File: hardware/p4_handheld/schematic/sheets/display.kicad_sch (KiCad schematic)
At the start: 0 parts

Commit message: hw(p4_handheld): display sheet wired to Waveshare 2.8in DSI panel
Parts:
- added C3: 10u, C0603, symbol Device:C
- added J3: FFC-15-1.0-FH12-class, FPC-SMD_FH12-15S-0.5SH-55, symbol PSP4H:Block2
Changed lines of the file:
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@@
     (comment 2 "Same-net labels connect; globals cross sheets")
   )
+  (symbol (lib_id "PSP4H:Block2") (at 35 35 0) (unit 1)
+    (exclude_from_sim no) (in_bom yes) (on_board yes) (dnp no) (fields_autoplaced)
+    (property "Reference" "J3" (at 35 29 0)
+      (effects (font (size 1.27 1.27))))
+    (property "Value" "FFC-15-1.0-FH12-class" (at 35 41 0)
+      (effects (font (size 1.27 1.27))))
+    (property "Footprint" "FPC-SMD_FH12-15S-0.5SH-55" (at 35 35 0)
+      (effects (font (size 1.27 1.27)) hide))
+    (property "Datasheet" "~" (at 35 35 0)
+      (effects (font (size 1.27 1.27)) hide))
+    (property "Gate" "GATE-PANEL-FFC-CONTACT" (at 35 35 0)
+      (effects (font (size 1.27 1.27)) hide))
+    (property "LCSC" "C2832207" (at 35 35 0)
+      (effects (font (size 1.27 1.27)) hide))
+    (property "MPN" "FH12-15S-0.5SH(55)" (at 35 35 0)
+      (effects (font (size 1.27 1.27)) hide))
+    (instances (project "card" (path "/p4_handheld/sheets/display" (reference "J3") (unit 1))))
+  )
+  (label "+3V3_PANEL" (at 53 32.5 0) (fields_autoplaced)
+    (effects (font (size 1.27 1.27)) (justify left)))
+  (label "+3V3_PANEL" (at 53 32.5 0) (fields_autoplaced)
+    (effects (font (size 1.27 1.27)) (justify left)))
+  (label "GND" (at 53 30 0) (fields_autoplaced)
+    (effects (font (size 1.27 1.27)) (justify left)))
+  (label "GND" (at 53 37.5 0) (fields_autoplaced)
+    (effects (font (size 1.27 1.27)) (justify left)))
+  (label "GND" (at 53 32.5 0) (fields_autoplaced)
+    (effects (font (size 1.27 1.27)) (justify left)))
+  (label "GND" (at 53 32.5 0) (fields_autoplaced)
+    (effects (font (size 1.27 1.27)) (justify left)))
+  (label "GND" (at 53 32.5 0) (fields_autoplaced)
+    (effects (font (size 1.27 1.27)) (justify left)))
+  (label "I2C_SDA" (at 53 32.5 0) (fields_autoplaced)
+    (effects (font (size 1.27 1.27)) (justify left)))
+  (label "I2C_SCL" (at 53 32.5 0) (fields_autoplaced)
+    (effects (font (size 1.27 1.27)) (justify left)))
+  (label "DSI_D1_N" (at 53 32.5 0) (fields_autoplaced)
+    (effects (font (size 1.27 1.27)) (justify left)))
+  (label "DSI_D1_P" (at 53 35 0) (fields_autoplaced)
+    (effects (font (size 1.27 1.27)) (justify left)))
+  (label "DSI_CLK_N" (at 53 40 0) (fields_autoplaced)
+    (effects (font (size 1.27 1.27)) (justify left)))
+  (label "DSI_CLK_P" (at 53 30 0) (fields_autoplaced)
+    (effects (font (size 1.27 1.27)) (justify left)))
+  (label "DSI_D0_N" (at 53 35 0) (fields_autoplaced)
+    (effects (font (size 1.27 1.27)) (justify left)))
+  (label "DSI_D0_P" (at 53 37.5 0) (fields_autoplaced)
+    (effects (font (size 1.27 1.27)) (justify left)))
+  (symbol (lib_id "Device:C") (at 80 35 0) (unit 1)
+    (exclude_from_sim no) (in_bom yes) (on_board yes) (dnp no) (fields_autoplaced)
+    (property "Reference" "C3" (at 80 29 0)
+      (effects (font (size 1.27 1.27))))
+    (property "Value" "10u" (at 80 41 0)
+      (effects (font (size 1.27 1.27))))
+    (property "Footprint" "C0603" (at 80 35 0)
+      (effects (font (size 1.27 1.27)) hide))
+    (property "Datasheet" "~" (at 80 35 0)
+      (effects (font (size 1.27 1.27)) hide))
+    (property "LCSC" "C19702" (at 80 35 0)
+      (effects (font (size 1.27 1.27)) hide))
+    (property "MPN" "CL10A106KP8NNNC" (at 80 35 0)
+      (effects (font (size 1.27 1.27)) hide))
+    (instances (project "card" (path "/p4_handheld/sheets/display" (reference "C3") (unit 1))))
+  )
+  (label "+3V3_PANEL" (at 98 30 0) (fields_autoplaced)
+    (effects (font (size 1.27 1.27)) (justify left)))
+  (label "GND" (at 98 32.5 0) (fields_autoplaced)
+    (effects (font (size 1.27 1.27)) (justify left)))
+  (global_label "+3V3_PANEL" (shape input) (at 280 20 0) (fields_autoplaced)
+    (effects (font (size 1.27 1.27)) (justify left))
+    (property "Intersheetrefs" "${INTERSHEET_REFS}" (at 280 20 0)
+      (effects (font (size 1.27 1.27)) hide))
+  )
+  (global_label "GND" (shape input) (at 280 26 0) (fields_autoplaced)
+    (effects (font (size 1.27 1.27)) (justify left))
+    (property "Intersheetrefs" "${INTERSHEET_REFS}" (at 280 26 0)
+      (effects (font (size 1.27 1.27)) hide))
+  )
+  (global_label "I2C_SDA" (shape input) (at 280 32 0) (fields_autoplaced)
+    (effects (font (size 1.27 1.27)) (justify left))
+    (property "Intersheetrefs" "${INTERSHEET_REFS}" (at 280 32 0)
+      (effects (font (size 1.27 1.27)) hide))
+  )
+  (global_label "I2C_SCL" (shape input) (at 280 38 0) (fields_autoplaced)
+    (effects (font (size 1.27 1.27)) (justify left))
+    (property "Intersheetrefs" "${INTERSHEET_REFS}" (at 280 38 0)
+      (effects (font (size 1.27 1.27)) hide))
+  )
+  (global_label "DSI_D1_N" (shape input) (at 280 44 0) (fields_autoplaced)
+    (effects (font (size 1.27 1.27)) (justify left))
+    (property "Intersheetrefs" "${INTERSHEET_REFS}" (at 280 44 0)
+      (effects (font (size 1.27 1.27)) hide))
+  )
+  (global_label "DSI_D1_P" (shape input) (at 280 50 0) (fields_autoplaced)
+    (effects (font (size 1.27 1.27)) (justify left))
+    (property "Intersheetrefs" "${INTERSHEET_REFS}" (at 280 50 0)
+      (effects (font (size 1.27 1.27)) hide))
+  )
+  (global_label "DSI_CLK_N" (shape input) (at 280 56 0) (fields_autoplaced)
+    (effects (font (size 1.27 1.27)) (justify left))
+    (property "Intersheetrefs" "${INTERSHEET_REFS}" (at 280 56 0)
+      (effects (font (size 1.27 1.27)) hide))
+  )
+  (global_label "DSI_CLK_P" (shape input) (at 280 62 0) (fields_autoplaced)
+    (effects (font (size 1.27 1.27)) (justify left))
+    (property "Intersheetrefs" "${INTERSHEET_REFS}" (at 280 62 0)
+      (effects (font (size 1.27 1.27)) hide))
+  )
+  (global_label "DSI_D0_N" (shape input) (at 280 68 0) (fields_autoplaced)
+    (effects (font (size 1.27 1.27)) (justify left))
+    (property "Intersheetrefs" "${INTERSHEET_REFS}" (at 280 68 0)
+      (effects (font (size 1.27 1.27)) hide))
+  )
+  (global_label "DSI_D0_P" (shape input) (at 280 74 0) (fields_autoplaced)
+    (effects (font (size 1.27 1.27)) (justify left))
+    (property "Intersheetrefs" "${INTERSHEET_REFS}" (at 280 74 0)
+      (effects (font (size 1.27 1.27)) hide))
+  )
 )

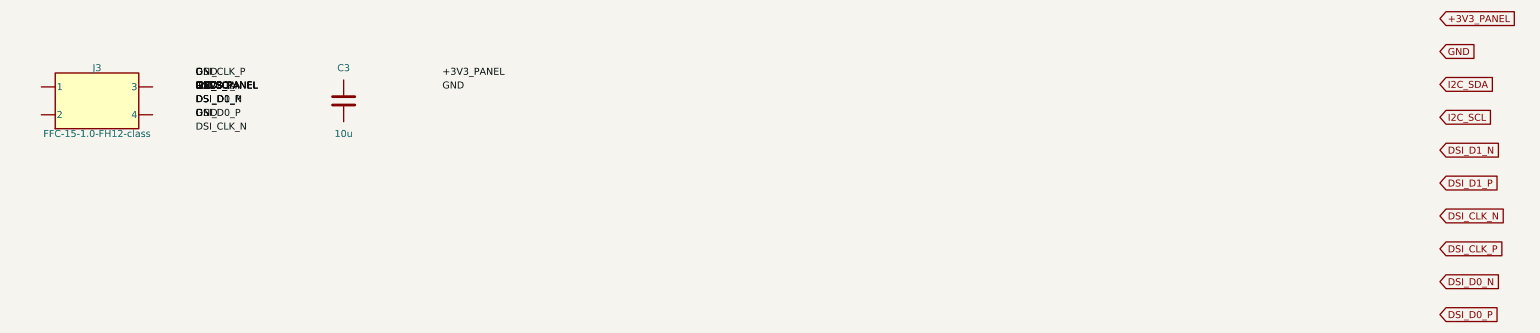
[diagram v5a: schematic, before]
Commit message: hw(p4_handheld): ERC-clean schematic engine (real pins, on-endpoint labels, project symbol lib)
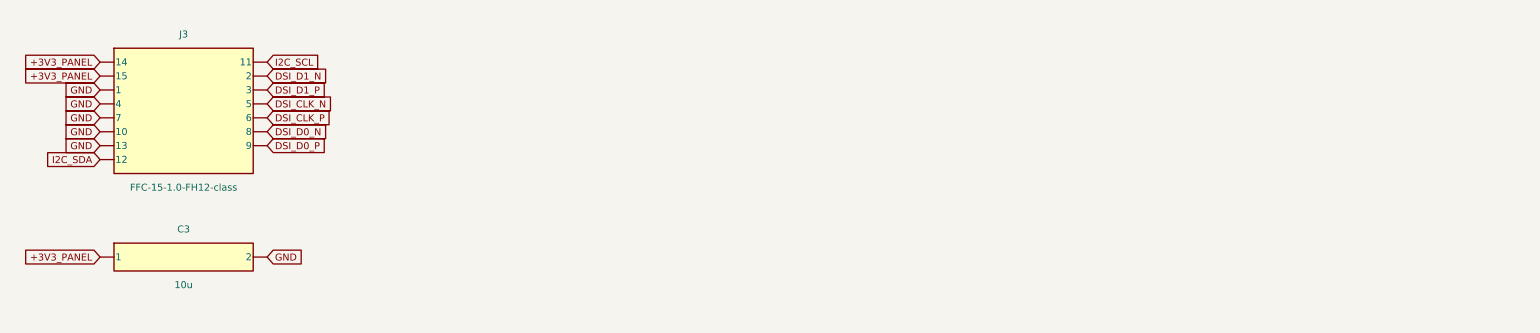
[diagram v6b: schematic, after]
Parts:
- removed C3: 10u, C0603, symbol Device:C
- removed J3: FFC-15-1.0-FH12-class, FPC-SMD_FH12-15S-0.5SH-55, symbol PSP4H:Block2
- added C3: 10u, symbol PSP4H:SYM_C3
- added J3: FFC-15-1.0-FH12-class, symbol PSP4H:SYM_J3
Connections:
- net +3V3_PANEL: now also C3.1, J3.14, J3.15
- net DSI_CLK_N: now also J3.5
- net DSI_D0_N: now also J3.8
- new net DSI_CLK_P: J3.6
- new net DSI_D0_P: J3.9
- new net DSI_D1_N: J3.2
- new net DSI_D1_P: J3.3
- new net GND: C3.2, J3.1, J3.10, J3.13, J3.4, J3.7
- new net I2C_SCL: J3.11
- new net I2C_SDA: J3.12
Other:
- title: PuzzleScript Card — display -> PuzzleScript P4 Handheld — display
